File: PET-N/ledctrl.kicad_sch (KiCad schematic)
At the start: 9 parts, among them J7 AVR-ISP-6, U1 LSF0204Q, U8 ATmega32A-A

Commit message: more layout work
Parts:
- added C1, C19, C2, C20, C21, C22, C23, C24, C25, C26, C27, C28, C29, C3, C4, C5, C6: 100u, Capacitor_SMD:C_1206_3216Metric_Pad1.33x1.80mm_HandSolder, symbol Device:C_Polarized
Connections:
- net GND: now also C1.2, C19.2, C2.2, C20.2, C21.2, C22.2, C23.2, C24.2, C25.2, C26.2, C27.2, C28.2, C29.2, C3.2, C4.2, C5.2, C6.2
- net VCC: now also C1.1, C19.1, C2.1, C20.1, C21.1, C22.1, C23.1, C24.1, C25.1, C26.1, C27.1, C28.1, C29.1, C3.1, C4.1, C5.1, C6.1

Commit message: almost done routing; last checks still open
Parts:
- added C31: 100n, Capacitor_SMD:C_0805_2012Metric_Pad1.18x1.45mm_HandSolder, symbol Device:C
- added C32, C33: 100u, Capacitor_SMD:C_1206_3216Metric_Pad1.33x1.80mm_HandSolder, symbol Device:C_Polarized
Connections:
- net GND: now also C31.2, C32.2, C33.2
- net VCC: now also C31.1, C32.1, C33.1
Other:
- note added: "(C) 2020,2021 Steve J. Gray (C) 2025 André Fachat"
- note added: "CBM-KEYB-PETN-3.0-20251005"
- note added: "LED Controller: - listens to I2C - runs light programs - programs the LEDS using L0-7"

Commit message: hopefully final schem and layout for 3.0A
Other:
- note added: "CBM-KEYB-PETN-3.0A-20251011"
- note removed: "CBM-KEYB-PETN-3.0-20251005"
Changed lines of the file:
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@@
 		)
 	)
-	(text "CBM-KEYB-PETN-3.0-20251005"
+	(text "CBM-KEYB-PETN-3.0A-20251011"
 		(exclude_from_sim no)
 		(at 230.378 172.72 0)

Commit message: as sent to production
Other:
- note added: "CBM-KEYB-PETN-3.0A-20251014"
- note removed: "CBM-KEYB-PETN-3.0A-20251011"
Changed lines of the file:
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@@
 		)
 	)
-	(text "CBM-KEYB-PETN-3.0A-20251011"
+	(text "CBM-KEYB-PETN-3.0A-20251014"
 		(exclude_from_sim no)
 		(at 230.378 172.72 0)

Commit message: first run on r3.1
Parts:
- added R1, R2: 2k2, Resistor_SMD:R_0603_1608Metric, symbol Device:R
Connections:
- net SCL: now also R1.2
- net SDA: now also R2.2
- net VCC: now also R1.1, R2.1
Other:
- note added: "(C) 2020, 2021 Steve J. Gray (C) 2025, 2026 André Fachat"
- note added: "CBM-KEYB-PETN-3.1A-20260130"
- note removed: "(C) 2020,2021 Steve J. Gray (C) 2025 André Fachat"
- note removed: "CBM-KEYB-PETN-3.0A-20251014"

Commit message: working on new layout
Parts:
- added D79: 1N4448, Diode_SMD:D_SOD-323_HandSoldering, symbol PCM_Diode_AKL:1N4448
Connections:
- net /RES: now also D79.2 (A); no longer J7.5 (~{RST})
- new net: D79.1 (K), J7.5 (~{RST})
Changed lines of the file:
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@@
 	)
 	(junction
+		(at 95.25 184.15)
+		(diameter 0)
+		(color 0 0 0 0)
+	)
+	(junction
 		(at 256.54 92.71)
 		(diameter 0)
@@
 	(wire
 		(pts
-			(xy 95.25 191.135) (xy 95.25 177.165)
+			(xy 95.25 191.135) (xy 95.25 184.15)
 		)
 		(stroke
@@
 	(wire
 		(pts
+			(xy 85.725 184.15) (xy 95.25 184.15)
+		)
+		(stroke
+			(width 0)
+			(type default)
+		)
+	)
+	(wire
+		(pts
 			(xy 234.95 106.68) (xy 256.54 106.68)
 		)
@@
 	(wire
 		(pts
-			(xy 95.25 177.165) (xy 71.12 177.165)
-		)
-		(stroke
-			(width 0)
-			(type default)
-		)
-	)
-	(wire
-		(pts
 			(xy 265.43 109.22) (xy 270.51 109.22)
 		)
@@
 	(wire
 		(pts
+			(xy 93.98 177.165) (xy 95.25 177.165)
+		)
+		(stroke
+			(width 0)
+			(type default)
+		)
+	)
+	(wire
+		(pts
 			(xy 207.01 104.14) (xy 207.01 111.76)
 		)
@@
 	(wire
 		(pts
+			(xy 71.12 177.165) (xy 86.36 177.165)
+		)
+		(stroke
+			(width 0)
+			(type default)
+		)
+	)
+	(wire
+		(pts
 			(xy 180.34 44.45) (xy 193.04 44.45)
 		)
@@
 	(wire
 		(pts
+			(xy 95.25 184.15) (xy 95.25 177.165)
+		)
+		(stroke
+			(width 0)
+			(type default)
+		)
+	)
+	(wire
+		(pts
 			(xy 238.76 116.84) (xy 238.76 118.11)
 		)
@@
 		)
 	)
+	(global_label "{slash}RESLED"
+		(shape input)
+		(at 85.725 184.15 180)
+		(fields_autoplaced yes)
+		(effects
+			(font
+				(size 1.27 1.27)
+			)
+			(justify right)
+		)
+		(property "Intersheetrefs" "${INTERSHEET_REFS}"
+			(at 74.9879 184.15 0)
+			(effects
+				(font
+					(size 1.27 1.27)
+				)
+				(justify right)
+				(hide yes)
+			)
+		)
+	)
 	(global_label "{slash}RES"
 		(shape input)
@@
 					(unit 1)
 				)
+			)
+		)
+	)
+	(symbol
+		(lib_id "PCM_Diode_AKL:1N4448")
+		(at 90.17 177.165 180)
+		(unit 1)
+		(exclude_from_sim no)
+		(in_bom yes)
+		(on_board yes)
+		(dnp no)
+		(fields_autoplaced yes)
+		(property "Reference" "D79"
+			(at 90.17 170.815 0)
+			(effects
+				(font
+					(size 1.27 1.27)
+				)
+			)
+		)
+		(property "Value" "1N4448"
+			(at 90.17 173.355 0)
+			(effects
+				(font
+					(size 1.27 1.27)
+				)
+			)
+		)
+		(property "Footprint" "Diode_SMD:D_SOD-323_HandSoldering"
+			(at 90.17 177.165 0)
+			(effects
+				(font
+					(size 1.27 1.27)
+				)
+				(hide yes)
+			)
+		)
+		(property "Datasheet" "https://datasheet.octopart.com/1N4448TR-ON-Semiconductor-datasheet-42765246.pdf"
+			(at 90.17 177.165 0)
+			(effects
+				(font
+					(size 1.27 1.27)
+				)
+				(hide yes)
+			)
+		)
+		(property "Description" "DO-35 Diode, Small Signal, Fast Switching, 75V, 150mA, 4ns, Alternate KiCad Library"
+			(at 90.17 177.165 0)
+			(effects
+				(font
+					(size 1.27 1.27)
+				)
+				(hide yes)
+			)
+		)
+		(pin "1"
+		)
+		(pin "2"
+		)
+		(instances
+			(project "petkn"
+				(path "/a0727808-af70-4056-b2ee-ab828c2acfbd/a39429aa-8c2f-45e6-a7a0-8f38ed5853cf"
+					(reference "D79")
+					(unit 1)
+				)

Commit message: layout work
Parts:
- added D81: 1N4448, Diode_SMD:D_SOD-323_HandSoldering, symbol PCM_Diode_AKL:1N4448
- added R5: 10k, Resistor_SMD:R_0603_1608Metric, symbol Device:R
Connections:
- net VCC: now also R5.2
- net /RES: now also D81.2 (A), R5.1
- new net /RESLED: D81.1 (K)
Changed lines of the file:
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@@
 	)
 	(junction
-		(at 127 183.515)
+		(at 95.25 183.515)
 		(diameter 0)
 		(color 0 0 0 0)
@@
 	)
 	(junction
+		(at 127 183.515)
+		(diameter 0)
+		(color 0 0 0 0)
+	)
+	(junction
 		(at 167.64 55.88)
 		(diameter 0)
@@
 	)
 	(junction
+		(at 112.395 183.515)
+		(diameter 0)
+		(color 0 0 0 0)
+	)
+	(junction
 		(at 256.54 106.68)
 		(diameter 0)
@@
 	)
 	(junction
-		(at 95.25 184.15)
-		(diameter 0)
-		(color 0 0 0 0)
-	)
-	(junction
 		(at 256.54 92.71)
 		(diameter 0)
@@
 	)
 	(junction
+		(at 95.25 187.96)
+		(diameter 0)
+		(color 0 0 0 0)
+	)
+	(junction
 		(at 218.44 44.45)
 		(diameter 0)
@@
 	(wire
 		(pts
-			(xy 95.25 191.135) (xy 95.25 184.15)
+			(xy 95.25 177.165) (xy 95.25 183.515)
 		)
 		(stroke
@@
 	(wire
 		(pts
+			(xy 95.25 183.515) (xy 99.06 183.515)
+		)
+		(stroke
+			(width 0)
+			(type default)
+		)
+	)
+	(wire
+		(pts
 			(xy 207.01 104.14) (xy 212.09 104.14)
 		)
@@
 	(wire
 		(pts
-			(xy 85.725 184.15) (xy 95.25 184.15)
+			(xy 234.95 106.68) (xy 256.54 106.68)
 		)
 		(stroke
@@
 	(wire
 		(pts
-			(xy 234.95 106.68) (xy 256.54 106.68)
+			(xy 207.01 100.33) (xy 207.01 104.14)
 		)
 		(stroke
@@
 	(wire
 		(pts
-			(xy 207.01 100.33) (xy 207.01 104.14)
+			(xy 112.395 183.515) (xy 112.395 180.975)
+		)
+		(stroke
+			(width 0)
+			(type default)
+		)
+	)
+	(wire
+		(pts
+			(xy 95.25 183.515) (xy 95.25 187.96)
 		)
 		(stroke
@@
 	(wire
 		(pts
-			(xy 127 183.515) (xy 127 179.705)
-		)
-		(stroke
-			(width 0)
-			(type default)
-		)
-	)
-	(wire
-		(pts
 			(xy 147.32 26.67) (xy 167.64 26.67)
 		)
@@
 	(wire
 		(pts
+			(xy 79.375 187.96) (xy 86.36 187.96)
+		)
+		(stroke
+			(width 0)
+			(type default)
+		)
+	)
+	(wire
+		(pts
 			(xy 150.495 40.64) (xy 167.64 40.64)
 		)
@@
 	(wire
 		(pts
+			(xy 127 179.705) (xy 127 183.515)
+		)
+		(stroke
+			(width 0)
+			(type default)
+		)
+	)
+	(wire
+		(pts
 			(xy 180.34 44.45) (xy 193.04 44.45)
 		)
@@
 	(wire
 		(pts
-			(xy 95.25 184.15) (xy 95.25 177.165)
-		)
-		(stroke
-			(width 0)
-			(type default)
-		)
-	)
-	(wire
-		(pts
 			(xy 238.76 116.84) (xy 238.76 118.11)
 		)
@@
 	(wire
 		(pts
+			(xy 95.25 187.96) (xy 95.25 191.135)
+		)
+		(stroke
+			(width 0)
+			(type default)
+		)
+	)
+	(wire
+		(pts
 			(xy 167.64 44.45) (xy 167.64 46.99)
 		)
@@
 	(wire
 		(pts
-			(xy 121.92 183.515) (xy 127 183.515)
+			(xy 112.395 183.515) (xy 127 183.515)
 		)
 		(stroke
@@
 	(wire
 		(pts
+			(xy 93.98 187.96) (xy 95.25 187.96)
+		)
+		(stroke
+			(width 0)
+			(type default)
+		)
+	)
+	(wire
+		(pts
 			(xy 218.44 26.67) (xy 231.14 26.67)
 		)
@@
 	(wire
 		(pts
+			(xy 106.68 183.515) (xy 112.395 183.515)
+		)
+		(stroke
+			(width 0)
+			(type default)
+		)
+	)
+	(wire
+		(pts
 			(xy 231.14 44.45) (xy 231.14 46.99)
 		)
@@
 	(global_label "{slash}RESLED"
 		(shape input)
-		(at 85.725 184.15 180)
+		(at 79.375 187.96 180)
 		(fields_autoplaced yes)
 		(effects
@@
 		)
 		(property "Intersheetrefs" "${INTERSHEET_REFS}"
-			(at 74.9879 184.15 0)
+			(at 68.6379 187.96 0)
 			(effects
 				(font
@@
 	)
 	(symbol
+		(lib_id "Device:R")
+		(at 102.87 183.515 90)
+		(unit 1)
+		(exclude_from_sim no)
+		(in_bom yes)
+		(on_board yes)
+		(dnp no)
+		(fields_autoplaced yes)
+		(property "Reference" "R5"
+			(at 102.87 177.165 90)
+			(effects
+				(font
+					(size 1.27 1.27)
+				)
+			)
+		)
+		(property "Value" "10k"
+			(at 102.87 179.705 90)
+			(effects
+				(font
+					(size 1.27 1.27)
+				)
+			)
+		)
+		(property "Footprint" "Resistor_SMD:R_0603_1608Metric"
+			(at 102.87 185.293 90)
+			(effects
+				(font
+					(size 1.27 1.27)
+				)
+				(hide yes)
+			)
+		)
+		(property "Datasheet" "~"
+			(at 102.87 183.515 0)
+			(effects
+				(font
+					(size 1.27 1.27)
+				)
+				(hide yes)
+			)
+		)
+		(property "Description" "Resistor"
+			(at 102.87 183.515 0)
+			(effects
+				(font
+					(size 1.27 1.27)
+				)
+				(hide yes)
+			)
+		)
+		(pin "2"
+		)
+		(pin "1"
+		)
+		(instances
+			(project "petkn"
+				(path "/a0727808-af70-4056-b2ee-ab828c2acfbd/a39429aa-8c2f-45e6-a7a0-8f38ed5853cf"
+					(reference "R5")
+					(unit 1)
+				)
+			)
+		)
+	)
+	(symbol
 		(lib_id "Device:C_Polarized")
 		(at 231.14 50.8 0)
@@
 	)
 	(symbol
+		(lib_id "PCM_Diode_AKL:1N4448")
+		(at 90.17 187.96 180)
+		(unit 1)
+		(exclude_from_sim no)
+		(in_bom yes)
+		(on_board yes)
+		(dnp no)
+		(fields_autoplaced yes)
+		(property "Reference" "D81"
+			(at 90.17 181.61 0)
+			(effects
+				(font
+					(size 1.27 1.27)
+				)
+			)
+		)
+		(property "Value" "1N4448"
+			(at 90.17 184.15 0)
+			(effects
+				(font
+					(size 1.27 1.27)
+				)
+			)
+		)
+		(property "Footprint" "Diode_SMD:D_SOD-323_HandSoldering"
+			(at 90.17 187.96 0)
+			(effects
+				(font
+					(size 1.27 1.27)
+				)
+				(hide yes)
+			)
+		)
+		(property "Datasheet" "https://datasheet.octopart.com/1N4448TR-ON-Semiconductor-datasheet-42765246.pdf"
+			(at 90.17 187.96 0)
+			(effects
+				(font
+					(size 1.27 1.27)
+				)
+				(hide yes)
+			)
+		)
+		(property "Description" "DO-35 Diode, Small Signal, Fast Switching, 75V, 150mA, 4ns, Alternate KiCad Library"
+			(at 90.17 187.96 0)
+			(effects
+				(font
+					(size 1.27 1.27)
+				)
+				(hide yes)
+			)
+		)
+		(pin "1"
+		)
+		(pin "2"
+		)
+		(instances
+			(project "petkn"
+				(path "/a0727808-af70-4056-b2ee-ab828c2acfbd/a39429aa-8c2f-45e6-a7a0-8f38ed5853cf"
+					(reference "D81")
+					(unit 1)
+				)
+			)
+		)
+	)
+	(symbol
 		(lib_id "Device:C_Polarized")
 		(at 135.255 49.53 0)
@@
 	(symbol
 		(lib_id "power:VCC")
-		(at 121.92 183.515 0)
+		(at 112.395 180.975 0)
 		(unit 1)
 		(exclude_from_sim no)
@@
 		(fields_autoplaced yes)
 		(property "Reference" "#PWR013"
-			(at 121.92 187.325 0)
+			(at 112.395 184.785 0)
 			(effects
 				(font
@@
 		)
 		(property "Value" "VCC"
-			(at 121.92 178.435 0)
+			(at 112.395 175.895 0)
 			(effects
 				(font
@@
 		)
 		(property "Footprint" ""
-			(at 121.92 183.515 0)
+			(at 112.395 180.975 0)
 			(effects
 				(font
@@
 		)
 		(property "Datasheet" ""
-			(at 121.92 183.515 0)
+			(at 112.395 180.975 0)
 			(effects
 				(font
@@
 		)
 		(property "Description" "Power symbol creates a global label with name \"VCC\""
-			(at 121.92 183.515 0)
+			(at 112.395 180.975 0)
 			(effects
 				(font

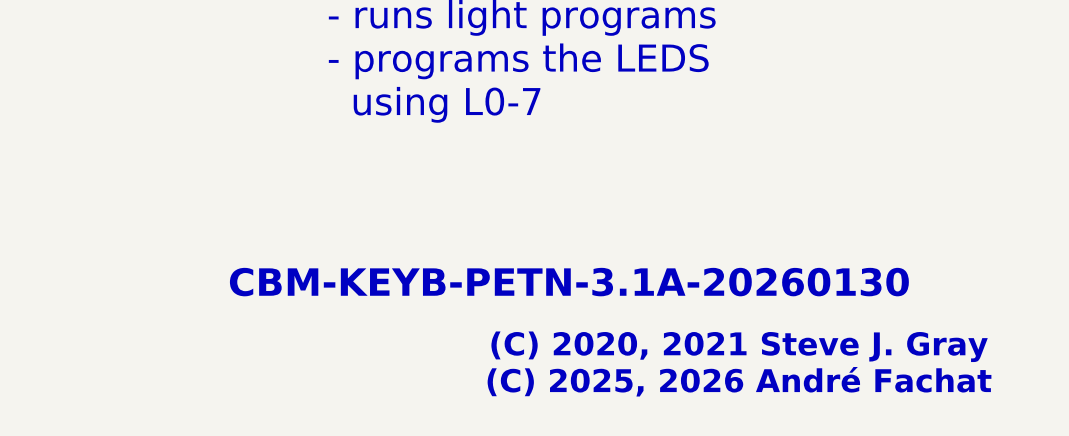
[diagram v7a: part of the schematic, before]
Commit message: add orientation marker for backlight LEDs and move to 3.1B
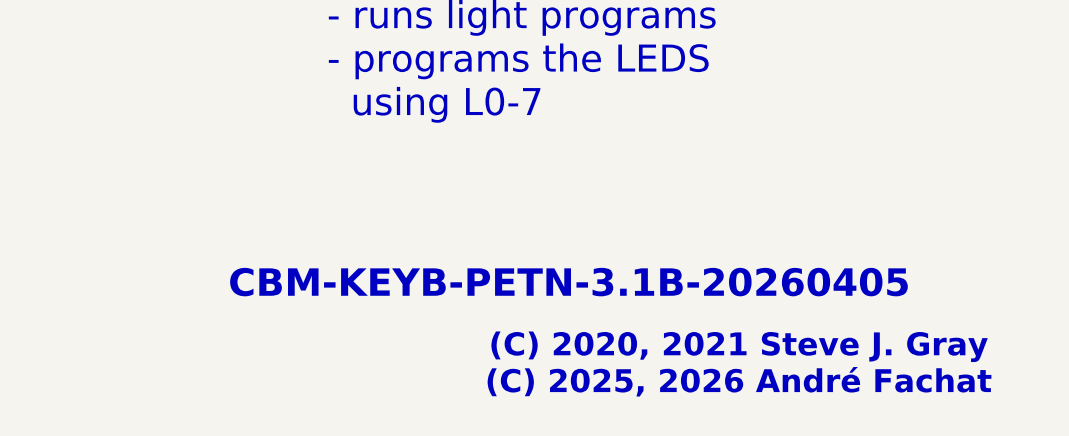
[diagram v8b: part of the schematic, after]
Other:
- note added: "CBM-KEYB-PETN-3.1B-20260405"
- note removed: "CBM-KEYB-PETN-3.1A-20260130"
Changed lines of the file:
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@@
 		)
 	)
-	(text "CBM-KEYB-PETN-3.1A-20260130"
+	(text "CBM-KEYB-PETN-3.1B-20260405"
 		(exclude_from_sim no)
 		(at 231.14 176.53 0)
